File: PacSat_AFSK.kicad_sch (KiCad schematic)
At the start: 4 parts

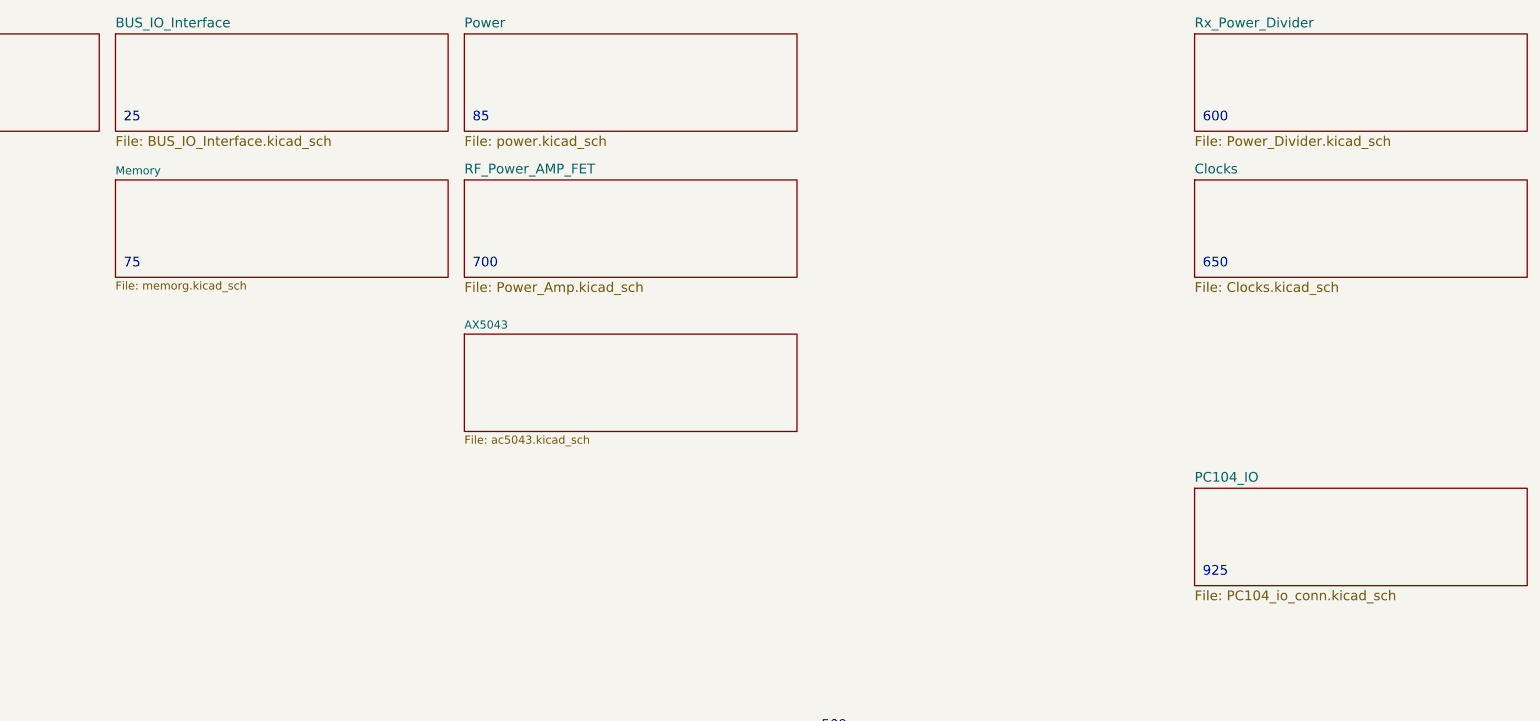
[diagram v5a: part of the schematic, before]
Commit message: Rework hierarchical sheets
Signed-off-by: Corey Minyard <corey@minyard.net>
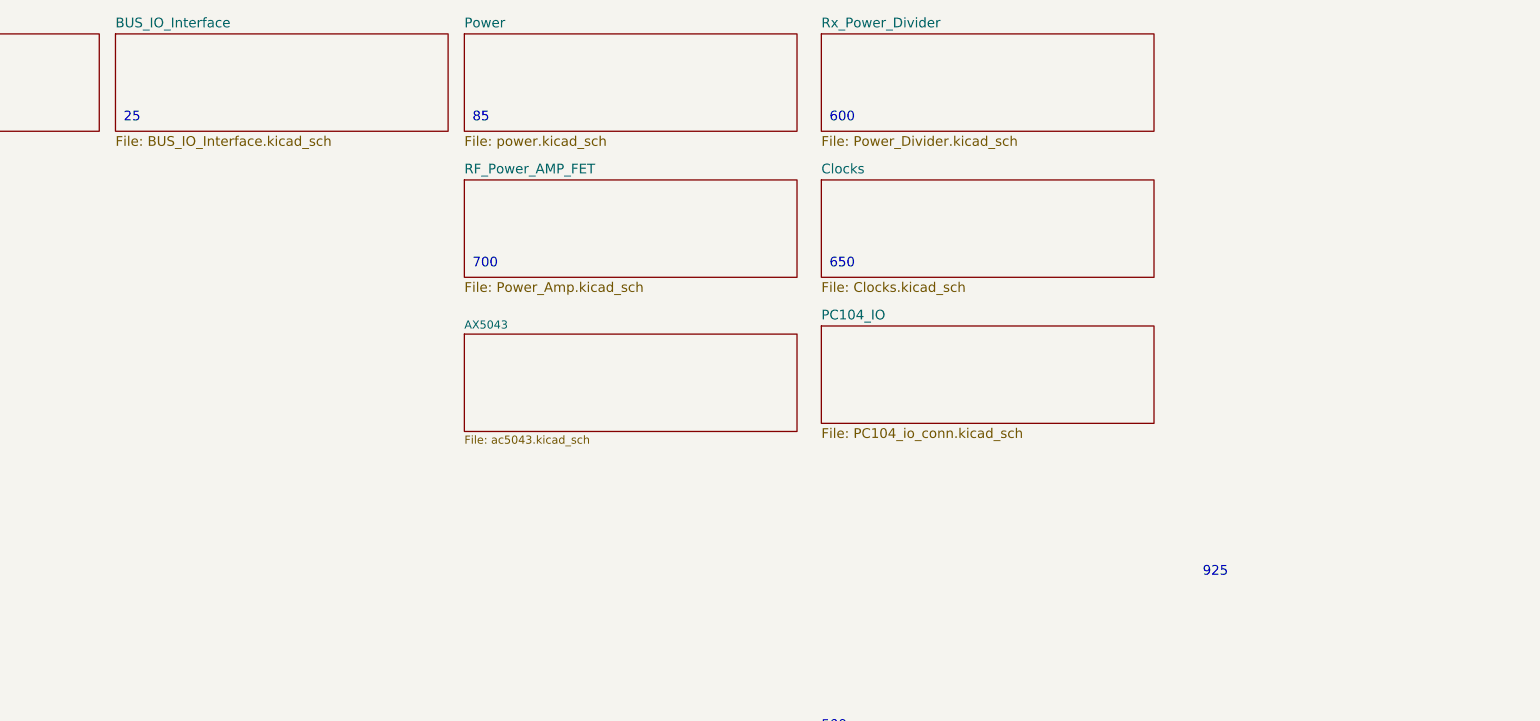
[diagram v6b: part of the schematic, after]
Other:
- removed sheet Memory
- note removed: "75"
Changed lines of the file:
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@@
 	(text "600"
 		(exclude_from_sim no)
-		(at 271.78 41.91 0)
+		(at 213.36 41.91 0)
 		(effects
 			(font
@@
 	(text "650"
 		(exclude_from_sim no)
-		(at 271.78 64.77 0)
-		(effects
-			(font
-				(size 1.524 1.524)
-			)
-			(justify left bottom)
-		)
-	)
-	(text "75"
-		(exclude_from_sim no)
-		(at 102.87 64.77 0)
+		(at 213.36 64.77 0)
 		(effects
 			(font
@@
 			(project "PacSat_AFSK"
 				(path "/cc9f42d2-6985-41ac-acab-5ab7b01c5b38"
-					(page "8")
+					(page "4")
 				)
 			)
@@
 	)
 	(sheet
-		(at 270.51 99.06)
+		(at 212.09 73.66)
 		(size 52.07 15.24)
 		(exclude_from_sim no)
@@
 		)
 		(property "Sheetname" "PC104_IO"
-			(at 270.51 98.2214 0)
+			(at 212.09 72.8214 0)
 			(effects
 				(font
@@
 		)
 		(property "Sheetfile" "PC104_io_conn.kicad_sch"
-			(at 270.51 114.9862 0)
+			(at 212.09 89.5862 0)
 			(effects
 				(font
@@
 			(project "PacSat_AFSK"
 				(path "/cc9f42d2-6985-41ac-acab-5ab7b01c5b38"
-					(page "15")
+					(page "14")
 				)
 			)
@@
 	)
 	(sheet
-		(at 101.6 50.8)
+		(at 212.09 27.94)
 		(size 52.07 15.24)
 		(exclude_from_sim no)
@@
 		(fields_autoplaced yes)
 		(stroke
-			(width 0.1524)
+			(width 0)
 			(type solid)
 		)
@@
 			(color 0 0 0 0.0000)
 		)
-		(property "Sheetname" "Memory"
-			(at 101.6 50.0884 0)
-			(effects
-				(font
-					(size 1.27 1.27)
+		(property "Sheetname" "Rx_Power_Divider"
+			(at 212.09 27.1014 0)
+			(effects
+				(font
+					(size 1.524 1.524)
 				)
 				(justify left bottom)
 			)
 		)
-		(property "Sheetfile" "memorg.kicad_sch"
-			(at 101.6 66.6246 0)
-			(effects
-				(font
-					(size 1.27 1.27)
+		(property "Sheetfile" "Power_Divider.kicad_sch"
+			(at 212.09 43.8662 0)
+			(effects
+				(font
+					(size 1.524 1.524)
 				)
 				(justify left top)
@@
 			(project "PacSat_AFSK"
 				(path "/cc9f42d2-6985-41ac-acab-5ab7b01c5b38"
-					(page "17")
+					(page "12")
 				)
 			)
@@
 	)
 	(sheet
-		(at 270.51 27.94)
+		(at 212.09 50.8)
 		(size 52.07 15.24)
 		(exclude_from_sim no)
@@
 			(color 0 0 0 0.0000)
 		)
-		(property "Sheetname" "Rx_Power_Divider"
-			(at 270.51 27.1014 0)
+		(property "Sheetname" "Clocks"
+			(at 212.09 49.9614 0)
 			(effects
 				(font
@@
 			)
 		)
-		(property "Sheetfile" "Power_Divider.kicad_sch"
-			(at 270.51 43.8662 0)
+		(property "Sheetfile" "Clocks.kicad_sch"
+			(at 212.09 66.7262 0)
 			(effects
 				(font
@@
 			(project "PacSat_AFSK"
 				(path "/cc9f42d2-6985-41ac-acab-5ab7b01c5b38"
-					(page "2")
-				)
-			)
-		)
-	)
-	(sheet
-		(at 270.51 50.8)
-		(size 52.07 15.24)
-		(exclude_from_sim no)
-		(in_bom yes)
-		(on_board yes)
-		(dnp no)
-		(fields_autoplaced yes)
-		(stroke
-			(width 0)
-			(type solid)
-		)
-		(fill
-			(color 0 0 0 0.0000)
-		)
-		(property "Sheetname" "Clocks"
-			(at 270.51 49.9614 0)
-			(effects
-				(font
-					(size 1.524 1.524)
-				)
-				(justify left bottom)
-			)
-		)
-		(property "Sheetfile" "Clocks.kicad_sch"
-			(at 270.51 66.7262 0)
-			(effects
-				(font
-					(size 1.524 1.524)
-				)
-				(justify left top)
-			)
-		)
-		(instances
-			(project "PacSat_AFSK"
-				(path "/cc9f42d2-6985-41ac-acab-5ab7b01c5b38"
-					(page "4")
+					(page "3")
 				)
 			)
@@
 			(project "PacSat_AFSK"
 				(path "/cc9f42d2-6985-41ac-acab-5ab7b01c5b38"
-					(page "12")
+					(page "2")
 				)
 			)
@@
 			(project "PacSat_AFSK"
 				(path "/cc9f42d2-6985-41ac-acab-5ab7b01c5b38"
-					(page "13")
+					(page "5")
 				)
 			)
@@
 			(project "PacSat_AFSK"
 				(path "/cc9f42d2-6985-41ac-acab-5ab7b01c5b38"
-					(page "14")
+					(page "13")
 				)
 			)
@@
 			(project "PacSat_AFSK"
 				(path "/cc9f42d2-6985-41ac-acab-5ab7b01c5b38"
-					(page "15")
-				)
-			)
+					(page "6")
+				)
+			)

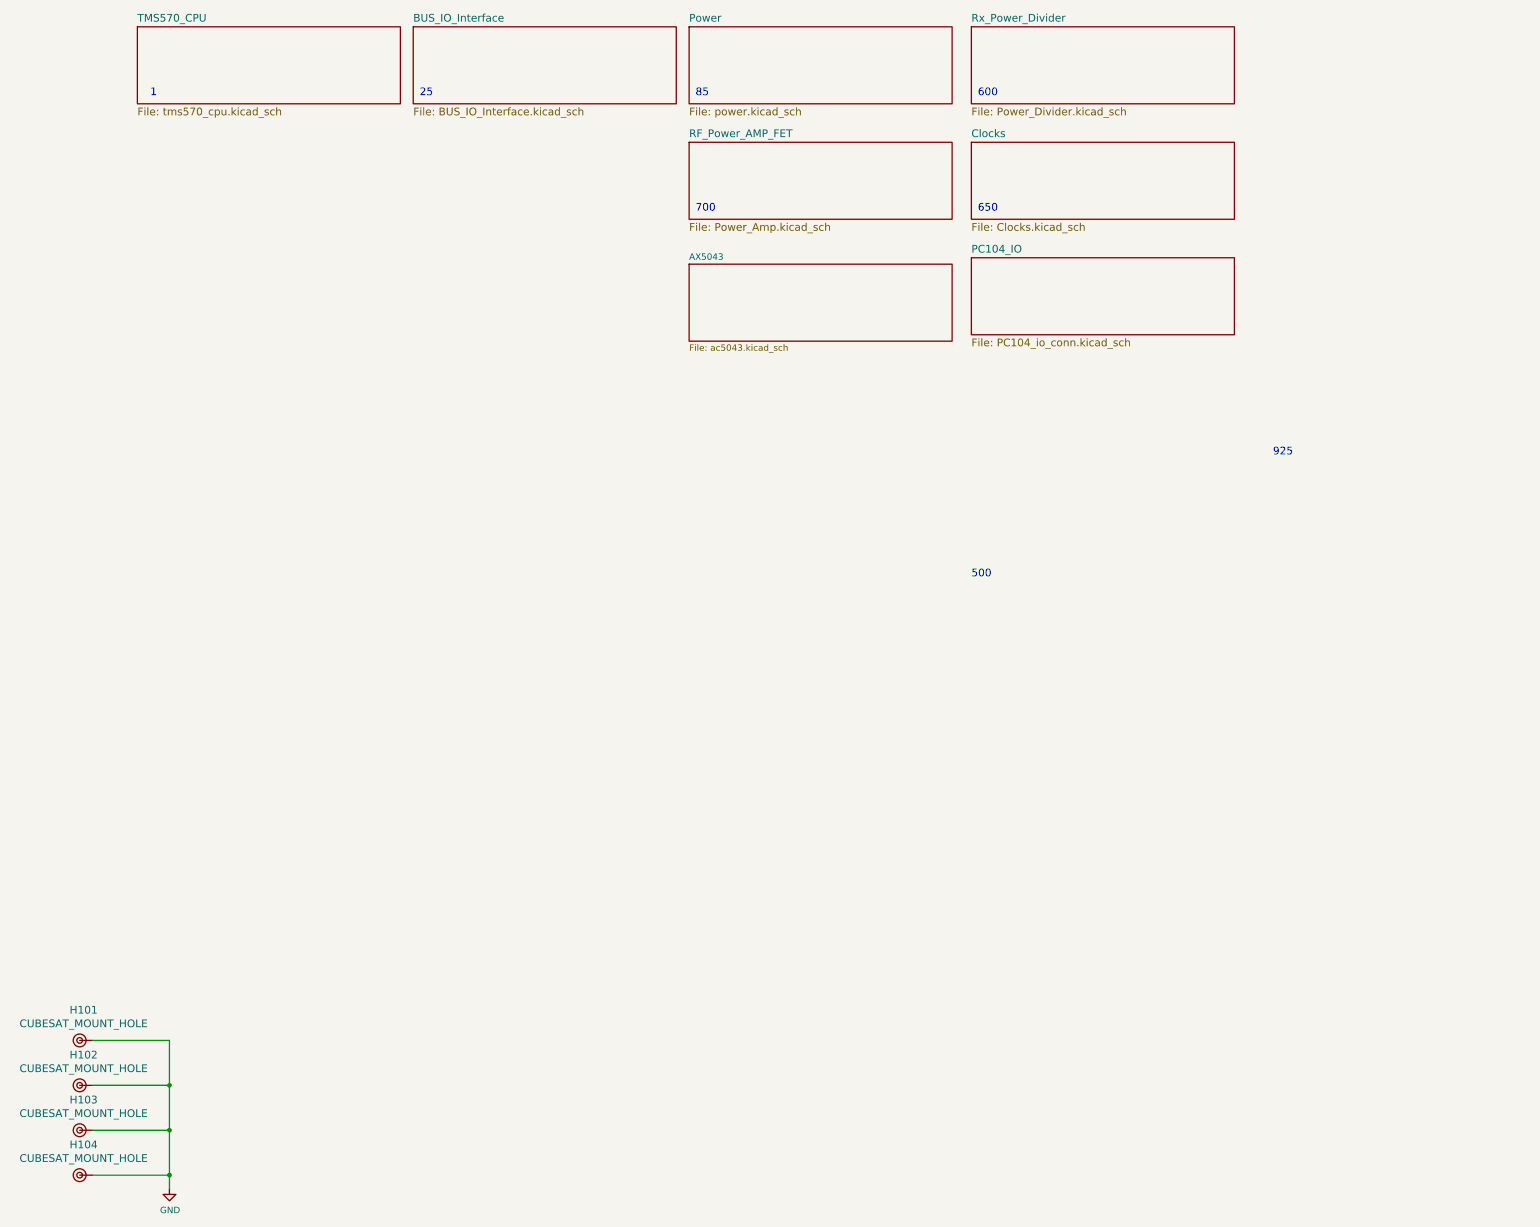
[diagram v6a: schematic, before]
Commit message: Re-annotate all parts
And get rid of the per-sheet annotation remarks.

Signed-off-by: Corey Minyard <corey@minyard.net>
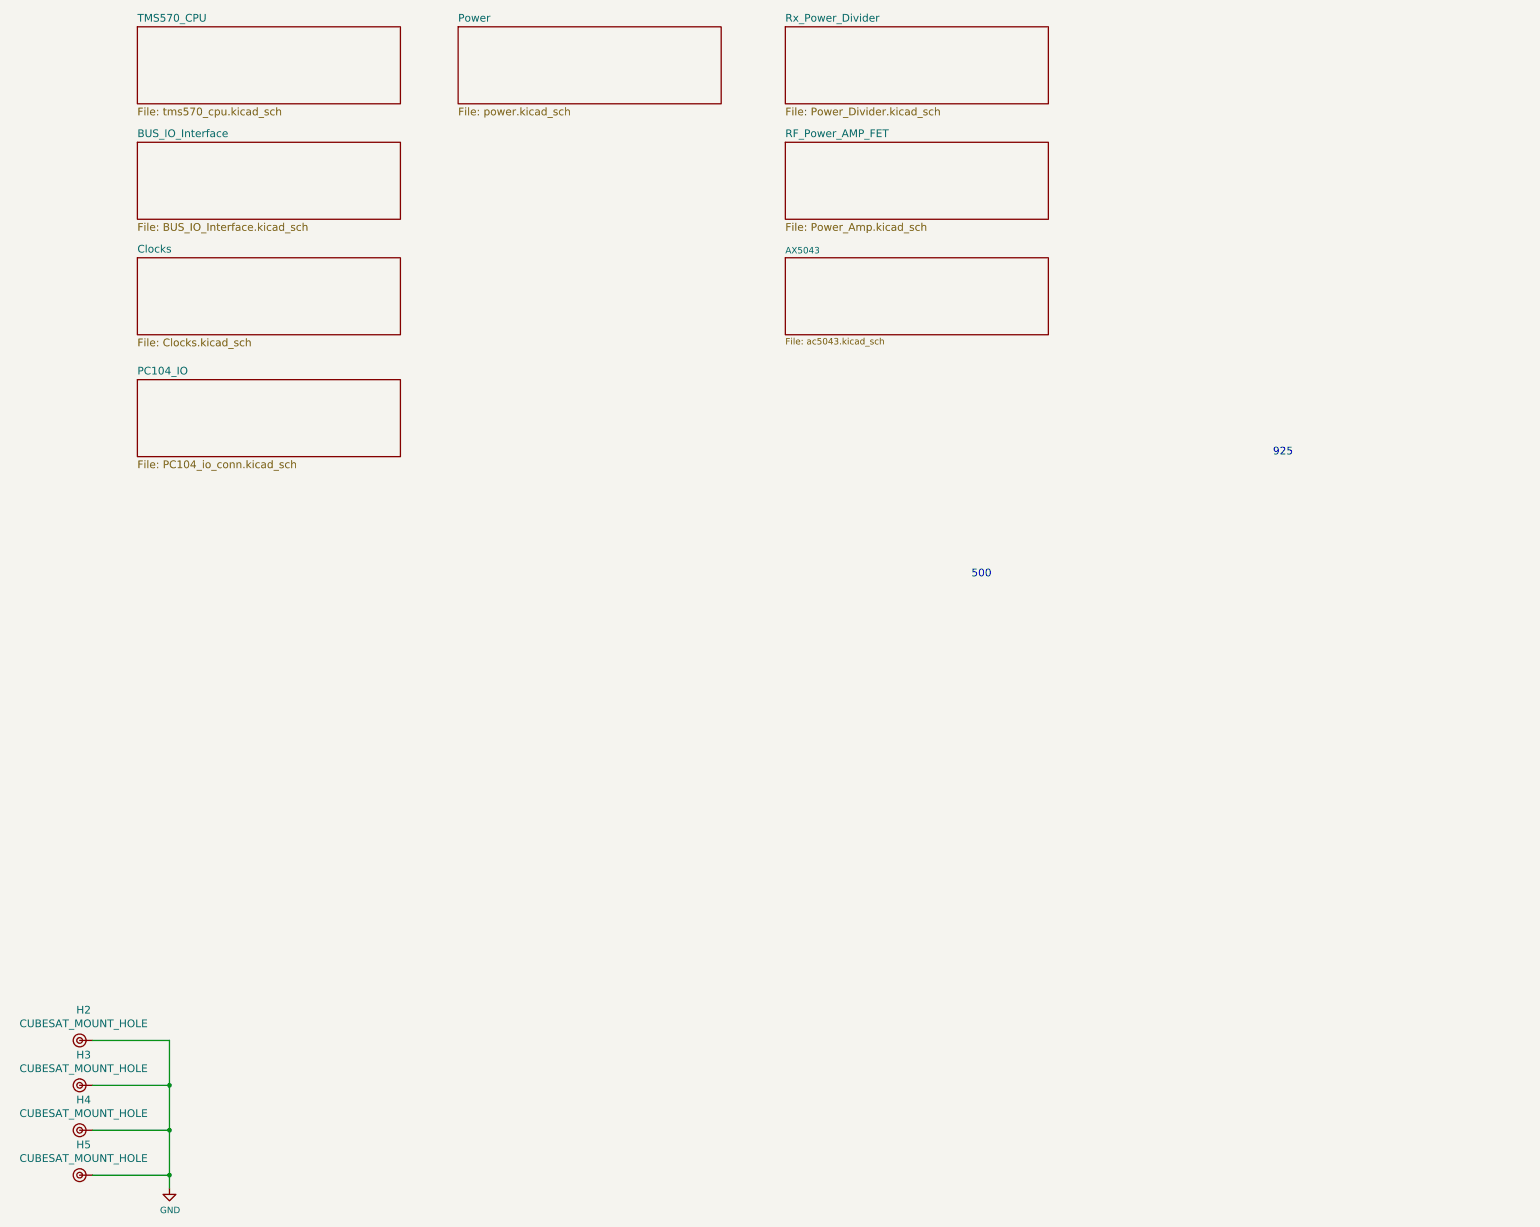
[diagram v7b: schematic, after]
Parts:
- renumbered H101 to H2, H102 to H3, H103 to H4, H104 to H5
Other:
- note removed: "1"
- note removed: "25"
- note removed: "600"
- note removed: "650"
- note removed: "700"
- note removed: "85"
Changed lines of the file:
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@@
 		(comment 1 "N5BRG")
-	)
-	(text "600"
-		(exclude_from_sim no)
-		(at 213.36 41.91 0)
-		(effects
-			(font
-				(size 1.524 1.524)
-			)
-			(justify left bottom)
-		)
-	)
-	(text "650"
-		(exclude_from_sim no)
-		(at 213.36 64.77 0)
-		(effects
-			(font
-				(size 1.524 1.524)
-			)
-			(justify left bottom)
-		)
 	)
 	(text "500"
@@
 		)
 	)
-	(text "700"
-		(exclude_from_sim no)
-		(at 157.48 64.77 0)
-		(effects
-			(font
-				(size 1.524 1.524)
-			)
-			(justify left bottom)
-		)
-	)
-	(text "1"
-		(exclude_from_sim no)
-		(at 49.53 41.91 0)
-		(effects
-			(font
-				(size 1.524 1.524)
-			)
-			(justify left bottom)
-		)
-	)
-	(text "25"
-		(exclude_from_sim no)
-		(at 102.87 41.91 0)
-		(effects
-			(font
-				(size 1.524 1.524)
-			)
-			(justify left bottom)
-		)
-	)
 	(text "925"
 		(exclude_from_sim no)
@@
 		)
 	)
-	(text "85"
-		(exclude_from_sim no)
-		(at 157.48 41.91 0)
-		(effects
-			(font
-				(size 1.524 1.524)
-			)
-			(justify left bottom)
-		)
-	)
 	(junction
 		(at 53.34 246.38)
@@
 		(on_board yes)
 		(dnp no)
-		(property "Reference" "H101"
+		(property "Reference" "H2"
 			(at 36.3474 222.5802 0)
 			(effects
@@
 			(project "PacSat_Dev_RevD_240614"
 				(path "/cc9f42d2-6985-41ac-acab-5ab7b01c5b38"
-					(reference "H101")
+					(reference "H2")
 					(unit 1)
 				)
@@
 		(on_board yes)
 		(dnp no)
-		(property "Reference" "H102"
+		(property "Reference" "H3"
 			(at 36.3474 231.4702 0)
 			(effects
@@
 			(project "PacSat_Dev_RevD_240614"
 				(path "/cc9f42d2-6985-41ac-acab-5ab7b01c5b38"
-					(reference "H102")
+					(reference "H3")
 					(unit 1)
 				)
@@
 		(on_board yes)
 		(dnp no)
-		(property "Reference" "H103"
+		(property "Reference" "H4"
 			(at 36.3474 240.3602 0)
 			(effects
@@
 			(project "PacSat_Dev_RevD_240614"
 				(path "/cc9f42d2-6985-41ac-acab-5ab7b01c5b38"
-					(reference "H103")
+					(reference "H4")
 					(unit 1)
 				)
@@
 		(on_board yes)
 		(dnp no)
-		(property "Reference" "H104"
+		(property "Reference" "H5"
 			(at 36.3474 249.2502 0)
 			(effects
@@
 			(project "PacSat_Dev_RevD_240614"
 				(path "/cc9f42d2-6985-41ac-acab-5ab7b01c5b38"
-					(reference "H104")
+					(reference "H5")
 					(unit 1)
 				)
@@
 		(on_board yes)
 		(dnp no)
-		(property "Reference" "#PWR0101"
+		(property "Reference" "#PWR02"
 			(at 53.34 264.16 0)
 			(effects
@@
 			(project "PacSat_Dev_RevD_240614"
 				(path "/cc9f42d2-6985-41ac-acab-5ab7b01c5b38"
-					(reference "#PWR0101")
+					(reference "#PWR02")
 					(unit 1)
 				)
@@
 	)
 	(sheet
-		(at 156.21 27.94)
+		(at 110.49 27.94)
 		(size 52.07 15.24)
 		(exclude_from_sim no)
@@
 		)
 		(property "Sheetname" "Power"
-			(at 156.21 27.1014 0)
+			(at 110.49 27.1014 0)
 			(effects
 				(font
@@
 		)
 		(property "Sheetfile" "power.kicad_sch"
-			(at 156.21 43.8662 0)
+			(at 110.49 43.8662 0)
 			(effects
 				(font
@@
 	)
 	(sheet
-		(at 212.09 73.66)
+		(at 46.99 97.79)
 		(size 52.07 15.24)
 		(exclude_from_sim no)
@@
 		)
 		(property "Sheetname" "PC104_IO"
-			(at 212.09 72.8214 0)
+			(at 46.99 96.9514 0)
 			(effects
 				(font
@@
 		)
 		(property "Sheetfile" "PC104_io_conn.kicad_sch"
-			(at 212.09 89.5862 0)
+			(at 46.99 113.7162 0)
 			(effects
 				(font
@@
 	)
 	(sheet
-		(at 212.09 27.94)
+		(at 175.26 27.94)
 		(size 52.07 15.24)
 		(exclude_from_sim no)
@@
 		)
 		(property "Sheetname" "Rx_Power_Divider"
-			(at 212.09 27.1014 0)
+			(at 175.26 27.1014 0)
 			(effects
 				(font
@@
 		)
 		(property "Sheetfile" "Power_Divider.kicad_sch"
-			(at 212.09 43.8662 0)
+			(at 175.26 43.8662 0)
 			(effects
 				(font
@@
 	)
 	(sheet
-		(at 212.09 50.8)
+		(at 46.99 73.66)
 		(size 52.07 15.24)
 		(exclude_from_sim no)
@@
 		)
 		(property "Sheetname" "Clocks"
-			(at 212.09 49.9614 0)
+			(at 46.99 72.8214 0)
 			(effects
 				(font
@@
 		)
 		(property "Sheetfile" "Clocks.kicad_sch"
-			(at 212.09 66.7262 0)
+			(at 46.99 89.5862 0)
 			(effects
 				(font
@@
 	)
 	(sheet
-		(at 101.6 27.94)
+		(at 46.99 50.8)
 		(size 52.07 15.24)
 		(exclude_from_sim no)
@@
 		)
 		(property "Sheetname" "BUS_IO_Interface"
-			(at 101.6 27.1014 0)
+			(at 46.99 49.9614 0)
 			(effects
 				(font
@@
 		)
 		(property "Sheetfile" "BUS_IO_Interface.kicad_sch"
-			(at 101.6 43.8662 0)
+			(at 46.99 66.7262 0)
 			(effects
 				(font
@@
 	)
 	(sheet
-		(at 156.21 50.8)
+		(at 175.26 50.8)
 		(size 52.07 15.24)
 		(exclude_from_sim no)
@@
 		)
 		(property "Sheetname" "RF_Power_AMP_FET"
-			(at 156.21 49.9614 0)
+			(at 175.26 49.9614 0)
 			(effects
 				(font
@@
 		)
 		(property "Sheetfile" "Power_Amp.kicad_sch"
-			(at 156.21 66.7262 0)
+			(at 175.26 66.7262 0)
 			(effects
 				(font
@@
 	)
 	(sheet
-		(at 156.21 74.93)
+		(at 175.26 73.66)
 		(size 52.07 15.24)
 		(exclude_from_sim no)
@@
 		)
 		(property "Sheetname" "AX5043"
-			(at 156.21 74.2184 0)
+			(at 175.26 72.9484 0)
 			(effects
 				(font
@@
 		)
 		(property "Sheetfile" "ac5043.kicad_sch"
-			(at 156.21 90.7546 0)
-			(effects
-				(font
+			(at 175.26 89.4846 0)
+			(effects
+				(font

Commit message: Lots of work on the documentation
Signed-off-by: Corey Minyard <corey@minyard.net>
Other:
- sheet AX5043: file ac5043.kicad_sch -> ax5043.kicad_sch
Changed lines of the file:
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@@
 			)
 		)
-		(property "Sheetfile" "ac5043.kicad_sch"
+		(property "Sheetfile" "ax5043.kicad_sch"
 			(at 175.26 89.4846 0)
 			(effects
